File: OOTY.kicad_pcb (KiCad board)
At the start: 4 copper layers, 85 x 55 mm, 197 parts, among them J1 TYPE-C-31-M-12, J2 SWD_HIL, J3 OLED 0.91in, J4 J_PWR, J5 J_DBG, J6 J_BUS, J7 J_UART_ANA, J8 J_IO, Q1 2N7002, Q2 2N7002, SW1 BTN1, SW2 BTN2, U1 TPD4E05U06DQAR, U10 INA226AIDGSR, U11 TLV9001IDBVR, U12 TPS2116DRLR, U13 AP2127K-ADJTRG1, U14 SN74LVC8T245PWR, U15 SN74LVC8T245PWR, U16 SN74LVC1T45DBVR, U17 SN74LVC1T45DBVR, U18 TCA9517ADGKR, U19 SN74LVC1T45DBVR, U2 USBLC6-2SC6, U20 TPD4E05U06DQAR, U21 TPD4E05U06DQAR, U22 TPD4E05U06DQAR, U23 TPD4E05U06DQAR, U24 TPD4E05U06DQAR, U25 TPD4E05U06DQAR, U26 TPD4E05U06DQAR, U27 TPD4E05U06DQAR, U3 TLV62569DBVR, U4 AP22653W6-7, U5 AP22653W6-7, U6 AP22653W6-7, U7 AP22653W6-7, U8 STM32G431MBT6, U9 INA226AIDGSR

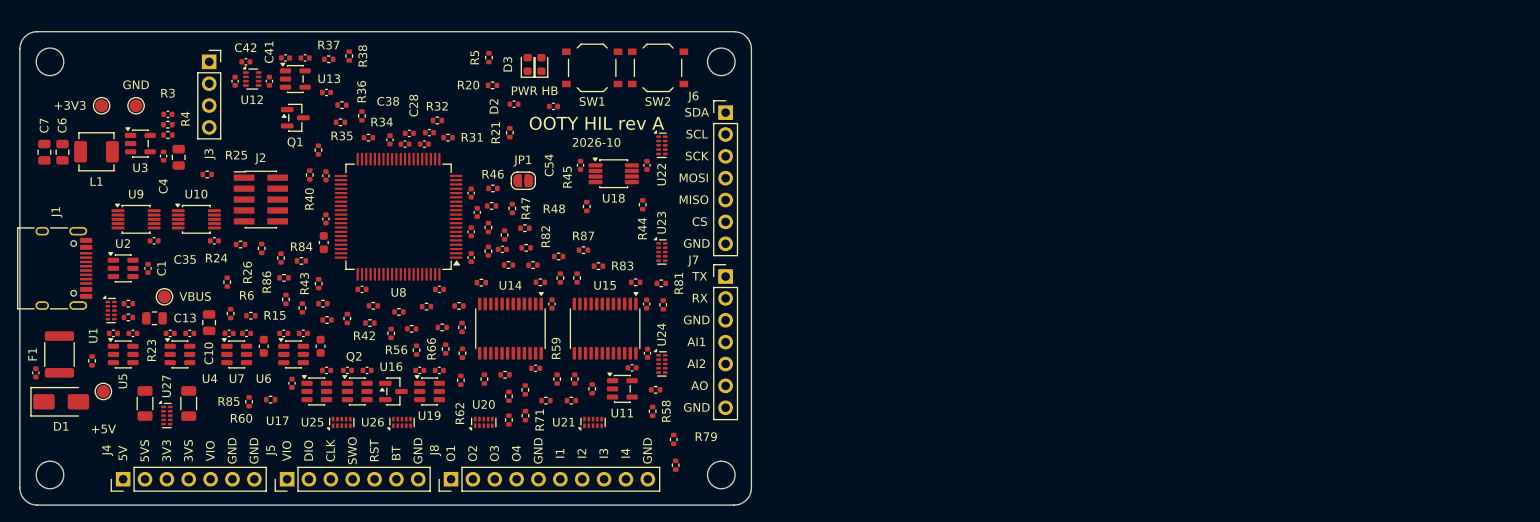
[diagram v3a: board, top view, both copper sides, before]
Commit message: fix: apply placement re-review (debug series resistors, USB corridor, shunt orientation, ILIM, EN_5V pull-up to 3V3)
- R83-R87 between the J_DBG drivers and their ESD; keepout corridor for USB D+/D-
- R22/R23 turned so current flows switch -> shunt -> header without crossing
- ILIM resistors next to pin 5 of each AP22653
- EN_5V pull-up to +3V3 instead of +5V (PD8 must not see 5 V while VDD is off)
- Silkscreen: a reference must be within 2 mm of its part and closer to it than to any
  other part (10 key references still without room, to finish with the next placement pass)

DRC with schematic parity: 0 errors. ERC: 0 errors.

Co-Authored-By: Claude Opus 5.5 <noreply@anthropic.com>
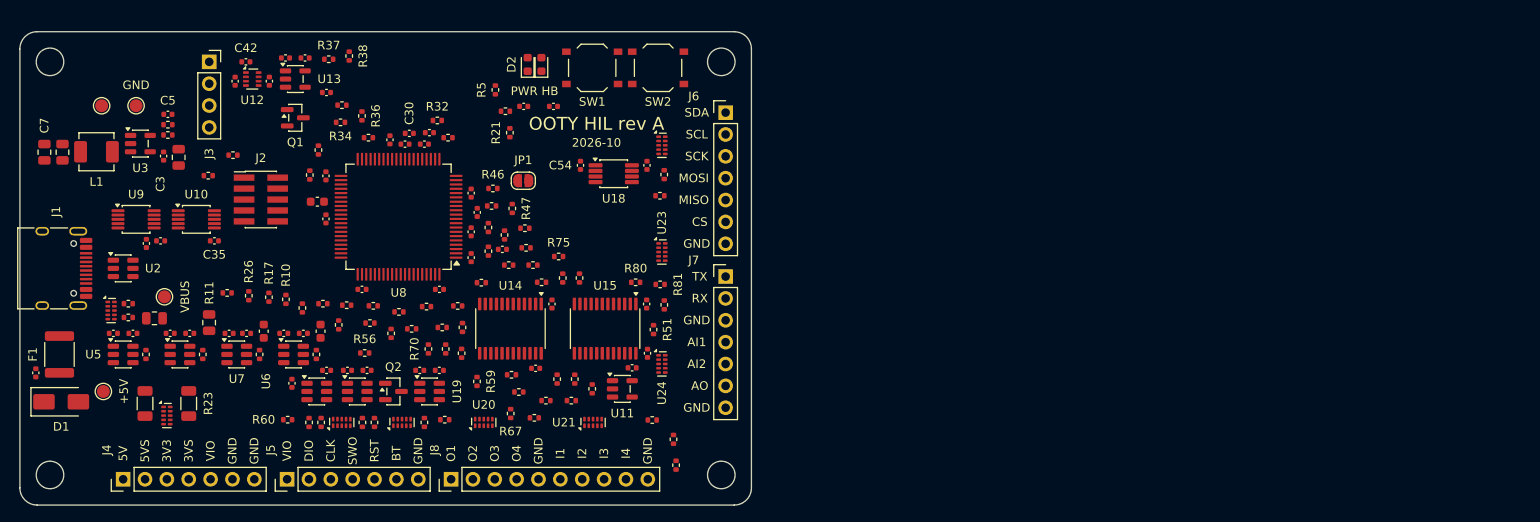
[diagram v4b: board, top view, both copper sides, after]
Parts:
- moved R83 37.0 mm to (135.0, 145.4), turned to 90 degrees
- moved R87 27.3 mm to (147.0, 145.4), turned to 90 degrees
- moved R82 24.6 mm to (176.2, 150.4)
- moved R86 22.0 mm to (141.2, 145.4)
- moved R84 20.1 mm to (139.8, 145.4), turned to 90 degrees
- moved R71 17.6 mm to (163.1, 128.6)
- moved R69 15.6 mm to (160.6, 129.1), turned to 0 degrees
- moved R70 15.1 mm to (147.5, 136.9), turned to 90 degrees
- moved R67 13.9 mm to (157.0, 144.4), turned to 90 degrees
- moved R58 13.8 mm to (159.8, 144.9), turned to 0 degrees
- moved R24 8.84 mm to (121.9, 116.7)
- moved R45 8.59 mm to (174.4, 119.1), turned to 0 degrees
- moved R73 8.39 mm to (165.0, 128.6), turned to 90 degrees
- moved R63 7.43 mm to (151.3, 137.4)
- moved R85 7.37 mm to (133.6, 145.4)
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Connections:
- R11 pad 2: +5V -> +3V3

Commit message: feat: place the dual-range blocks (TASK-012, in progress)
Power chain hand-placed between the limiters and J_PWR, comparators above the
limiter row, flip-flops and shunt amplifiers under the MCU, test points,
bypass bridges and unfitted capacitors on the bottom side. Bottom-side parts
handled by the placer and the silkscreen; Flip() fixed (footprint added to
the board first). DRC 0 errors, parity 0, decoupling 59/59.

Co-Authored-By: Claude Opus 5.5 <noreply@anthropic.com>
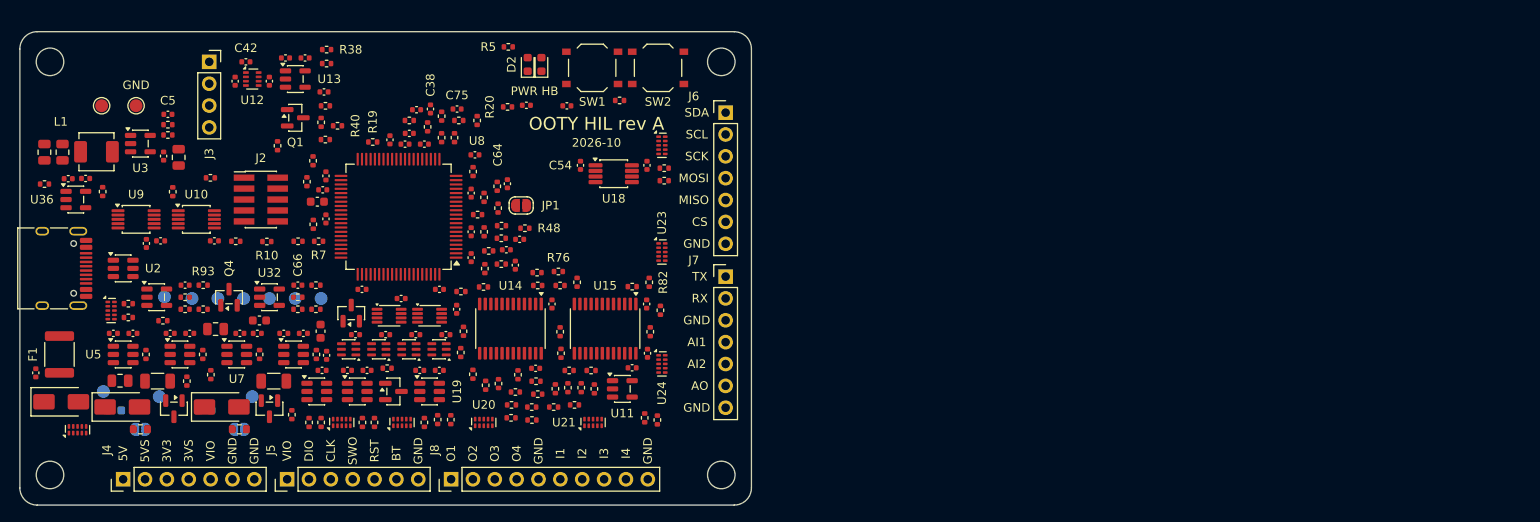
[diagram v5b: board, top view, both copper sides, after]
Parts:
- added C58: 1uF/25V X7R, Capacitor_SMD:C_0603_1608Metric, B.Cu at (111.0, 144.0)
- added C59: 100nF/50V, Capacitor_SMD:C_0402_1005Metric, F.Cu at (119.2, 129.4)
- added C60: 100nF/50V, Capacitor_SMD:C_0402_1005Metric, F.Cu at (144.3, 131.0)
- added C61: 100nF/50V, Capacitor_SMD:C_0402_1005Metric, F.Cu at (139.0, 135.2)
- added C62: 1nF/50V, Capacitor_SMD:C_0402_1005Metric, F.Cu at (135.2, 118.4)
- added C63: 100nF/50V, Capacitor_SMD:C_0402_1005Metric, F.Cu at (142.5, 135.2)
- added C64: 1nF/50V, Capacitor_SMD:C_0402_1005Metric, F.Cu at (152.9, 114.3)
- added C65: 1uF/25V X7R, Capacitor_SMD:C_0603_1608Metric, B.Cu at (121.5, 144.0)
- added C66: 100nF/50V, Capacitor_SMD:C_0402_1005Metric, F.Cu at (132.3, 129.4)
- added C67: 100nF/50V, Capacitor_SMD:C_0402_1005Metric, F.Cu at (150.8, 132.2)
- added C68: 100nF/50V, Capacitor_SMD:C_0402_1005Metric, F.Cu at (146.0, 135.2)
- added C69: 1nF/50V, Capacitor_SMD:C_0402_1005Metric, F.Cu at (157.6, 127.1)
- added C70: 100nF/50V, Capacitor_SMD:C_0402_1005Metric, F.Cu at (149.5, 135.2)
- added C71: 1nF/50V, Capacitor_SMD:C_0402_1005Metric, F.Cu at (158.1, 124.1)
- added C72: 100nF/50V, Capacitor_SMD:C_0402_1005Metric, F.Cu at (105.6, 117.1)
- added C73: 100nF/50V, Capacitor_SMD:C_0402_1005Metric, F.Cu at (107.6, 117.0)
- added C74: 100nF/50V, Capacitor_SMD:C_0402_1005Metric, F.Cu at (146.1, 109.1)
- added C75: 100nF/50V, Capacitor_SMD:C_0402_1005Metric, F.Cu at (150.8, 109.0)
- added D4: M7, Diode_SMD:D_SMA, F.Cu at (111.9, 143.6)
- added D5: M7, Diode_SMD:D_SMA, F.Cu at (123.5, 143.6)
- added JP2: BYPASS, Jumper:SolderJumper-2_P1.3mm_Open_RoundedPad1.0x1.5mm, B.Cu at (114.0, 146.2)
- added JP3: BYPASS, Jumper:SolderJumper-2_P1.3mm_Open_RoundedPad1.0x1.5mm, B.Cu at (125.5, 146.2)
- added Q3: AO3401A, Package_TO_SOT_SMD:SOT-23, F.Cu at (117.9, 143.8)
- added Q4: 2N7002, Package_TO_SOT_SMD:SOT-23, F.Cu at (124.3, 130.8)
- added Q5: AO3401A, Package_TO_SOT_SMD:SOT-23, F.Cu at (129.0, 143.8)
- added Q6: 2N7002, Package_TO_SOT_SMD:SOT-23, F.Cu at (138.5, 132.7)
- added R100: 1k, Resistor_SMD:R_0402_1005Metric, F.Cu at (132.3, 130.8)
- added R101: 100k, Resistor_SMD:R_0402_1005Metric, F.Cu at (132.3, 132.2)
- added R102: 10k, Resistor_SMD:R_0402_1005Metric, F.Cu at (134.4, 129.4)
- added R103: 100k, Resistor_SMD:R_0402_1005Metric, F.Cu at (154.5, 125.5)
- added R104: 100R, Resistor_SMD:R_0402_1005Metric, F.Cu at (155.9, 124.0)
- added R105: 100R, Resistor_SMD:R_0402_1005Metric, F.Cu at (155.9, 127.0)
- added R106: 30k, Resistor_SMD:R_0402_1005Metric, F.Cu at (102.9, 117.7)
- added R107: 1k, Resistor_SMD:R_0402_1005Metric, F.Cu at (109.6, 118.6)
- added R108: 100k, Resistor_SMD:R_0402_1005Metric, F.Cu at (145.2, 110.3)
- added R109: 100k, Resistor_SMD:R_0402_1005Metric, F.Cu at (149.0, 109.8)
- added R110: 100k, Resistor_SMD:R_0402_1005Metric, F.Cu at (151.0, 110.3)
- added R111: 100k, Resistor_SMD:R_0402_1005Metric, F.Cu at (153.1, 110.3)
- added R88: 100R 0.1%, Resistor_SMD:R_0603_1608Metric, F.Cu at (114.0, 146.2)
- added R89: 100k, Resistor_SMD:R_0402_1005Metric, F.Cu at (119.4, 140.6)
- added R90: 1k, Resistor_SMD:R_0402_1005Metric, F.Cu at (121.3, 132.2)
- added R91: 1k, Resistor_SMD:R_0402_1005Metric, F.Cu at (119.2, 130.8)
- added R92: 150k, Resistor_SMD:R_0402_1005Metric, F.Cu at (119.2, 132.2)
- added R93: 10k, Resistor_SMD:R_0402_1005Metric, F.Cu at (121.3, 129.4)
- added R94: 100k, Resistor_SMD:R_0402_1005Metric, F.Cu at (152.7, 116.2)
- added R95: 100R, Resistor_SMD:R_0402_1005Metric, F.Cu at (134.1, 115.0)
- added R96: 100R, Resistor_SMD:R_0402_1005Metric, F.Cu at (150.5, 112.3)
- added R97: 100R 0.1%, Resistor_SMD:R_0603_1608Metric, F.Cu at (125.5, 146.2)
- added R98: 100k, Resistor_SMD:R_0402_1005Metric, F.Cu at (131.6, 144.5)
- added R99: 1k, Resistor_SMD:R_0402_1005Metric, F.Cu at (134.4, 132.2)
- added TP10: RANGE_3V3SW, TestPoint:TestPoint_Pad_D1.5mm, B.Cu at (129.0, 131.0)
- added TP11: I_3V3SW_LO_AMP, TestPoint:TestPoint_Pad_D1.5mm, B.Cu at (132.0, 131.0)
- added TP12: I_3V3SW_HI_AMP, TestPoint:TestPoint_Pad_D1.5mm, B.Cu at (135.0, 131.0)
- added TP5: 5V_SW_MID, TestPoint:TestPoint_Pad_D1.5mm, B.Cu at (116.2, 142.4)
- added TP6: RANGE_5VSW, TestPoint:TestPoint_Pad_D1.5mm, B.Cu at (120.0, 131.0)
- added TP7: I_5VSW_LO_AMP, TestPoint:TestPoint_Pad_D1.5mm, B.Cu at (123.0, 131.0)
- added TP8: I_5VSW_HI_AMP, TestPoint:TestPoint_Pad_D1.5mm, B.Cu at (126.0, 131.0)
- added TP9: 3V3_SW_MID, TestPoint:TestPoint_Pad_D1.5mm, B.Cu at (127.0, 142.4)
- added U28: TLV7021DBVR, Package_TO_SOT_SMD:SOT-23-5, F.Cu at (115.9, 130.8)
- added U29: SN74LVC1G74DCUR, Package_SO:VSSOP-8_2.3x2mm_P0.5mm, F.Cu at (142.9, 133.0)
- added U30: INA190A2IDCKR, Package_TO_SOT_SMD:SOT-363_SC-70-6, F.Cu at (138.2, 136.9)
- added U31: INA190A2IDCKR, Package_TO_SOT_SMD:SOT-363_SC-70-6, F.Cu at (141.7, 136.9)
- added U32: TLV7021DBVR, Package_TO_SOT_SMD:SOT-23-5, F.Cu at (129.0, 130.8)
- added U33: SN74LVC1G74DCUR, Package_SO:VSSOP-8_2.3x2mm_P0.5mm, F.Cu at (147.6, 133.0)
- added U34: INA190A2IDCKR, Package_TO_SOT_SMD:SOT-363_SC-70-6, F.Cu at (145.2, 136.9)
- added U35: INA190A2IDCKR, Package_TO_SOT_SMD:SOT-363_SC-70-6, F.Cu at (148.7, 136.9)
- added U36: TLV9001IDBVR, Package_TO_SOT_SMD:SOT-23-5, F.Cu at (106.5, 119.5)
- TP1, TP2: moved to B.Cu
- moved R82 21.5 mm to (173.1, 129.1)
- moved R60 18.5 mm to (116.6, 133.6)
- moved R69 16.0 mm to (159.5, 145.1)
- moved R16 15.9 mm to (148.5, 145.1)
- moved R70 15.5 mm to (162.2, 141.5)
- moved R26 14.9 mm to (133.3, 117.4)
- moved R71 14.8 mm to (164.4, 143.4), turned to 0 degrees
- moved R43 14.3 mm to (151.2, 137.3), turned to 90 degrees
- moved R21 13.3 mm to (169.7, 108.0), turned to 0 degrees
- moved R68 13.2 mm to (157.1, 144.9)
- moved R65 13.1 mm to (157.1, 143.4)
- moved R56 12.7 mm to (150.1, 145.1), turned to 90 degrees
- moved R66 12.1 mm to (159.5, 143.6), turned to 0 degrees
- moved R13 11.8 mm to (134.1, 122.4), turned to 90 degrees
- moved R64 11.7 mm to (160.2, 142.1), turned to 0 degrees
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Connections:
- R22 pad 2: 5V_SW -> 5V_SW_MID
- R23 pad 2: 3V3_SW -> 3V3_SW_MID
- U10 pad 9: 3V3_SW -> 3V3_SW_MID
- U8 pad 22: VIO_PR1 -> I_5VSW_HI
- U8 pad 23: VIO_MODE -> V_3V3_DUT
- U8 pad 24: OUT4_MCU -> V_5V_DUT
- U8 pad 30: unconnected-(U8-PE7-Pad30) -> FAULT_5V
- U8 pad 31: unconnected-(U8-PE8-Pad31) -> FAULT_3V3SW
- U8 pad 32: unconnected-(U8-PE9-Pad32) -> OUT4_MCU
- U8 pad 36: unconnected-(U8-PE13-Pad36) -> VIO_VSEL
- U8 pad 37: unconnected-(U8-PE14-Pad37) -> VIO_PR1
- U8 pad 38: unconnected-(U8-PE15-Pad38) -> VIO_MODE
- U8 pad 45: VIO_VSEL -> I_5VSW_LO
- U8 pad 5: FAULT_3V3SW -> I_3V3SW_LO
- U8 pad 58: unconnected-(U8-PA10-Pad58) -> RANGE_CLK_5VSW
- U8 pad 6: FAULT_5V -> I_3V3SW_HI
- U8 pad 69: unconnected-(U8-PD0-Pad69) -> RANGE_5VSW
- U8 pad 70: unconnected-(U8-PD1-Pad70) -> RANGE_3V3SW
- U8 pad 73: unconnected-(U8-PB4-Pad73) -> RANGE_CLK_3V3SW
- U9 pad 9: 5V_SW -> 5V_SW_MID

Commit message: feat: finish the placement and silkscreen of TASK-012
Every key part has its reference (on top, or on B.SilkS under the part when the
top side is full); test points, bypass bridges and unfitted parts on the bottom
side; bottom renders and assembly drawing; NOTES updated. DRC 0 errors, parity 0,
decoupling 59/59.

Co-Authored-By: Claude Opus 5.5 <noreply@anthropic.com>
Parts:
- TP3, TP4: moved to B.Cu
- moved TP10 30.2 mm to (152.0, 111.5)
- moved TP6 27.9 mm to (140.0, 111.5)
- moved TP11 23.9 mm to (152.0, 118.0)
- moved TP7 21.4 mm to (140.0, 118.0)
- moved TP12 18.2 mm to (152.0, 124.5)
- moved TP8 15.4 mm to (140.0, 124.5)
- moved TP1 9.26 mm to (109.5, 136.5)
- moved TP2 6.04 mm to (105.0, 138.0)
- moved C58 2.50 mm to (110.3, 146.4)

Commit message: fix: apply the TASK-012 placement review
Flip-flop U29 next to its comparator (short /PRE), U33 next to U32, 2N7002
drivers under the MCU, amplifier row at a 4 mm pitch with the REF buffer next
to it, R60 back near the J_DBG series resistors, rail ESD under the J4 label,
ADC capacitors at PF0/PF1, test points outside the MCU body, routing room
between the two chains. DRC 0 errors, parity 0, decoupling 59/59.

Co-Authored-By: Claude Opus 5.5 <noreply@anthropic.com>
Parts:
- moved R106 58.2 mm to (160.4, 126.4)
- moved R107 53.8 mm to (162.9, 126.4), turned to 0 degrees
- moved C73 53.5 mm to (155.9, 140.1), turned to 90 degrees
- moved U36 51.2 mm to (153.0, 141.0)
- moved C72 50.9 mm to (155.4, 127.9)
- moved R94 39.9 mm to (116.7, 133.5), turned to 0 degrees
- moved TP10 32.9 mm to (130.0, 136.0)
- moved R43 27.9 mm to (134.7, 114.8), turned to 0 degrees
- moved R17 25.2 mm to (133.4, 117.3)
- moved R49 23.4 mm to (155.6, 116.5)
- moved C60 22.5 mm to (121.8, 130.8)
- moved R60 19.8 mm to (132.0, 146.0)
- moved Q4 19.4 mm to (143.6, 132.6)
- moved TP6 19.1 mm to (124.0, 122.0)
- moved U29 18.7 mm to (124.3, 130.9), turned to 90 degrees
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
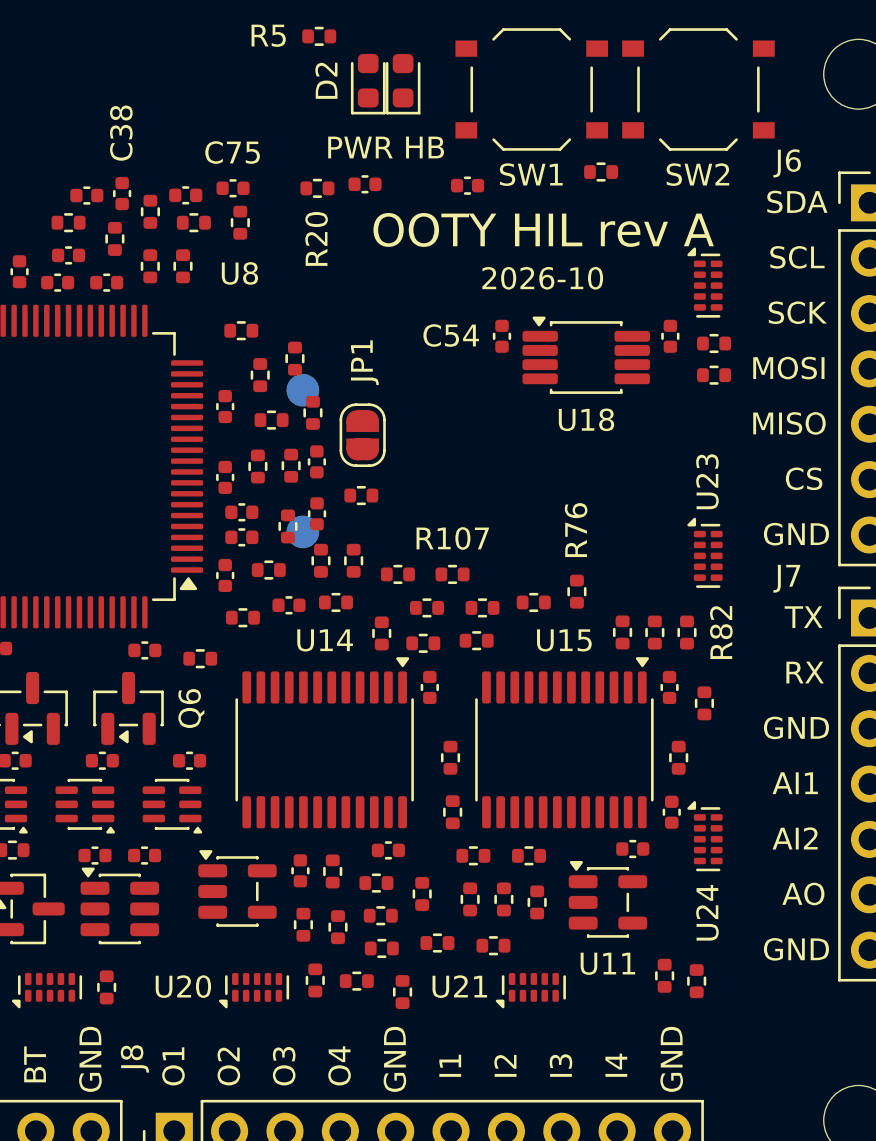
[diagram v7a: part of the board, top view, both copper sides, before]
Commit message: fix: TASK-012 counter-review (REF divider next to U36, series resistors back near J8)
Co-Authored-By: Claude Opus 5.5 <noreply@anthropic.com>
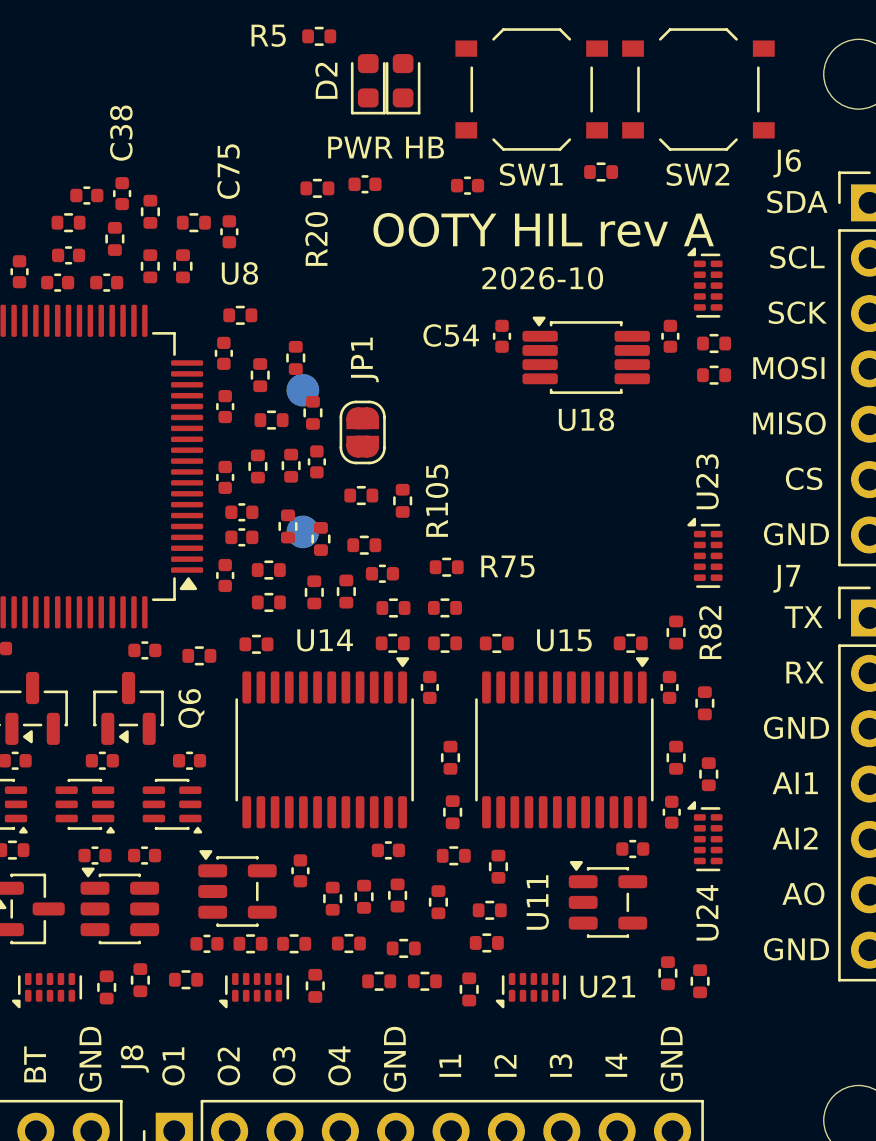
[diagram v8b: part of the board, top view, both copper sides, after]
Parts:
- moved R49 28.9 mm to (150.6, 145.1), turned to 0 degrees
- moved R107 19.3 mm to (153.6, 143.4)
- moved R68 18.9 mm to (154.4, 127.7), turned to 0 degrees
- moved R72 18.4 mm to (161.6, 145.1), turned to 0 degrees
- moved R106 17.6 mm to (155.6, 143.4)
- moved R66 17.2 mm to (160.2, 128.0)
- moved C72 16.0 mm to (151.6, 143.4)
- moved R71 15.6 mm to (164.4, 143.4)
- moved R50 15.3 mm to (156.5, 127.3)
- moved R16 15.0 mm to (148.5, 145.1), turned to 90 degrees
- moved R65 14.0 mm to (160.1, 129.6)
- moved R79 12.8 mm to (174.4, 132.4)
- moved R70 12.1 mm to (162.2, 141.5), turned to 90 degrees
- moved R76 9.99 mm to (158.8, 125.1), turned to 0 degrees
- moved R51 8.11 mm to (173.1, 134.9), turned to 90 degrees
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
